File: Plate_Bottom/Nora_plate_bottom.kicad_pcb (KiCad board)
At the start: 2 copper layers, 285 x 94.6 mm, 8 parts

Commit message: WIP ボトムプレートに切り取りをつけようとしている
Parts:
- added REF**: breakaway-mousebites, locallib:breakaway-mousebites, F.Cu at (185.2, 43.6)
- added REF**: breakaway-mousebites, locallib:breakaway-mousebites, F.Cu at (130.6, 43.6)

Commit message: WIP ボトムプレートに切り取りをつけ、さらに改造中
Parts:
- removed the REF** at (185.2, 43.6)
- REF**: footprint locallib:60_Outline_for_Bottom_USB_cutout_slit_closed_with_PICO -> locallib:60_Outline_Nora_with_PICO_
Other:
- outline, holes or cut-outs redrawn

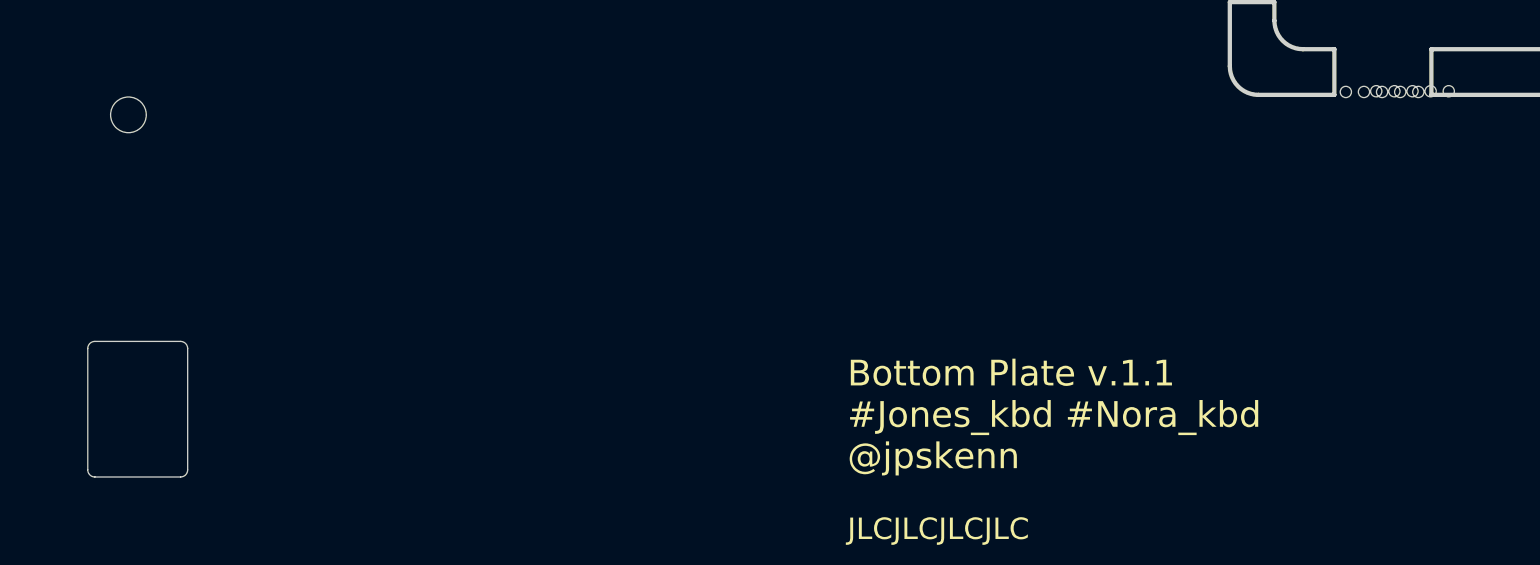
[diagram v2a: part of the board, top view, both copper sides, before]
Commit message: WIP リセットボタン穴など追加
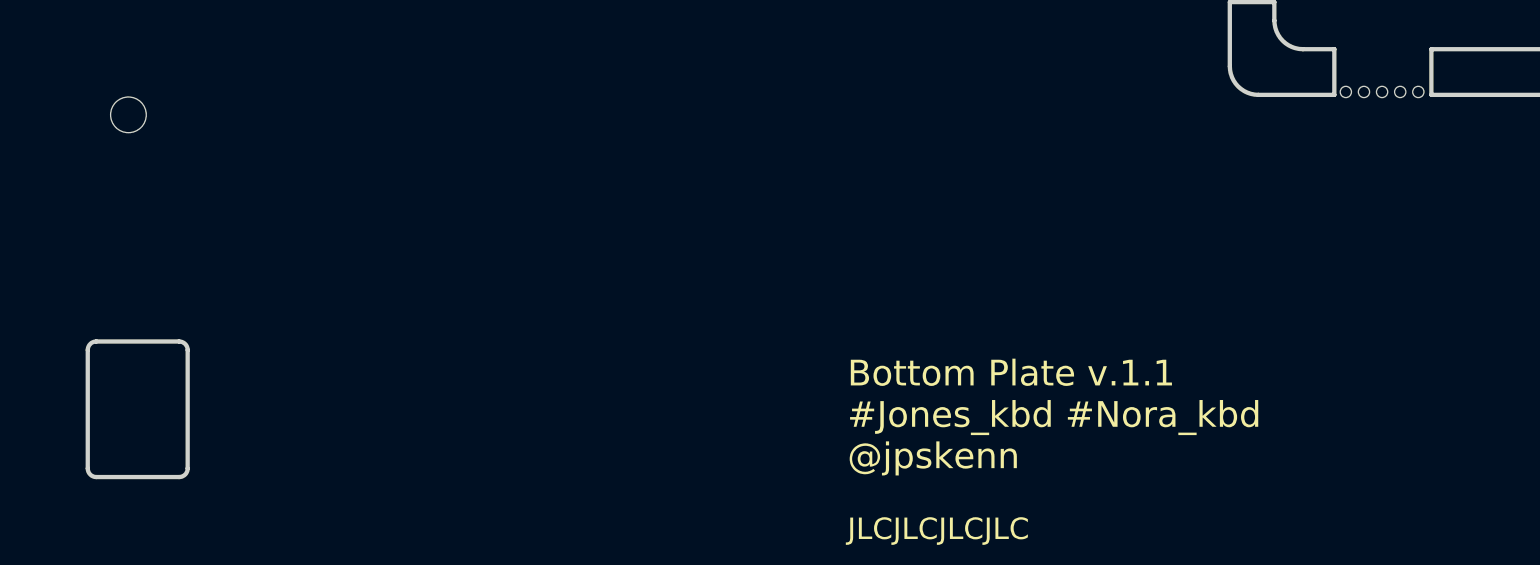
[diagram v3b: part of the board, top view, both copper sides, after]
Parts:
- removed the REF** at (130.6, 43.6)
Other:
- outline, holes or cut-outs redrawn

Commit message: ボトムプレート完成
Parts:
- removed the G*** at (183.0, 66.0)
- added G***: LOGO, locallib:Jones_logo_11.4x19.3, F.Cu at (185.0, 67.0)
- moved G*** 1.50 mm to (218.0, 67.5)
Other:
- outline, holes or cut-outs redrawn
- board text added: "Bottom Plate v.1.1 @jpskenn"
- board text removed: "Bottom Plate v.1.1 #Jones_kbd #Nora_kbd @jpskenn"

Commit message: 新しいロゴに変更 #61
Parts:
- G***: footprint locallib:Nora_logo_21.8*7.2 -> locallib:Nora_logo_21.8*7.7
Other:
- net class Default removed
- board text added: "Bottom Plate v.1.2 @jpskenn"
- board text removed: "Bottom Plate v.1.1 @jpskenn"
